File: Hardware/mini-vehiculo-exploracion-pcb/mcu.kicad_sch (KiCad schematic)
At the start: 20 parts, among them J3 UJ20-C-H-G-SMT-5-P16-TR

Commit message: update pcb4
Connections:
- net GND: now also J3.MP1, J3.MP2, J3.MP3, J3.MP4
- no-connect marks 10 -> 6
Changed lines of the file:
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@@
 	)
 	(junction
+		(at 69.85 110.49)
+		(diameter 0)
+		(color 0 0 0 0)
+	)
+	(junction
+		(at 69.85 113.03)
+		(diameter 0)
+		(color 0 0 0 0)
+	)
+	(junction
 		(at 77.47 33.02)
 		(diameter 0)
@@
 	)
 	(junction
+		(at 69.85 115.57)
+		(diameter 0)
+		(color 0 0 0 0)
+	)
+	(junction
 		(at 101.6 48.26)
 		(diameter 0)
@@
 	)
 	(no_connect
-		(at 67.31 110.49)
-	)
-	(no_connect
-		(at 67.31 115.57)
-	)
-	(no_connect
-		(at 67.31 113.03)
-	)
-	(no_connect
-		(at 67.31 107.95)
-	)
-	(no_connect
 		(at 71.12 55.88)
 	)
@@
 	(wire
 		(pts
+			(xy 69.85 110.49) (xy 69.85 113.03)
+		)
+		(stroke
+			(width 0)
+			(type default)
+		)
+	)
+	(wire
+		(pts
 			(xy 73.66 147.32) (xy 73.66 151.13)
 		)
@@
 	(wire
 		(pts
+			(xy 67.31 107.95) (xy 69.85 107.95)
+		)
+		(stroke
+			(width 0)
+			(type default)
+		)
+	)
+	(wire
+		(pts
 			(xy 67.31 102.87) (xy 71.12 102.87)
 		)
@@
 	(wire
 		(pts
+			(xy 69.85 107.95) (xy 69.85 110.49)
+		)
+		(stroke
+			(width 0)
+			(type default)
+		)
+	)
+	(wire
+		(pts
 			(xy 130.81 97.79) (xy 139.7 97.79)
 		)
@@
 	(wire
 		(pts
+			(xy 69.85 113.03) (xy 69.85 115.57)
+		)
+		(stroke
+			(width 0)
+			(type default)
+		)
+	)
+	(wire
+		(pts
 			(xy 101.6 62.23) (xy 104.14 62.23)
 		)
@@
 	(wire
 		(pts
+			(xy 69.85 115.57) (xy 69.85 118.11)
+		)
+		(stroke
+			(width 0)
+			(type default)
+		)
+	)
+	(wire
+		(pts
 			(xy 73.66 130.81) (xy 73.66 127)
 		)
@@
 	(wire
 		(pts
+			(xy 67.31 113.03) (xy 69.85 113.03)
+		)
+		(stroke
+			(width 0)
+			(type default)
+		)
+	)
+	(wire
+		(pts
 			(xy 137.16 118.11) (xy 137.16 120.65)
 		)
@@
 	(wire
 		(pts
+			(xy 67.31 110.49) (xy 69.85 110.49)
+		)
+		(stroke
+			(width 0)
+			(type default)
+		)
+	)
+	(wire
+		(pts
 			(xy 101.6 33.02) (xy 107.95 33.02)
 		)
@@
 	(wire
 		(pts
+			(xy 67.31 115.57) (xy 69.85 115.57)
+		)
+		(stroke
+			(width 0)
+			(type default)
+		)
+	)
+	(wire
+		(pts
 			(xy 77.47 113.03) (xy 85.09 113.03)
 		)
@@
 					(unit 1)
 				)
+			)
+		)
+	)
+	(symbol
+		(lib_id "power:GND")
+		(at 69.85 118.11 0)
+		(unit 1)
+		(exclude_from_sim no)
+		(in_bom yes)
+		(on_board yes)
+		(dnp no)
+		(fields_autoplaced yes)
+		(property "Reference" "#PWR013"
+			(at 69.85 124.46 0)
+			(effects
+				(font
+					(size 1.27 1.27)
+				)
+				(hide yes)
+			)
+		)
+		(property "Value" "GND"
+			(at 69.85 123.19 0)
+			(effects
+				(font
+					(size 1.27 1.27)
+				)
+			)
+		)
+		(property "Footprint" ""
+			(at 69.85 118.11 0)
+			(effects
+				(font
+					(size 1.27 1.27)
+				)
+				(hide yes)
+			)
+		)
+		(property "Datasheet" ""
+			(at 69.85 118.11 0)
+			(effects
+				(font
+					(size 1.27 1.27)
+				)
+				(hide yes)
+			)
+		)
+		(property "Description" "Power symbol creates a global label with name \"GND\" , ground"
+			(at 69.85 118.11 0)
+			(effects
+				(font
+					(size 1.27 1.27)
+				)
+				(hide yes)
+			)
+		)
+		(pin "1"
+		)
+		(instances
+			(project ""
+				(path "/3cb3b833-c38f-47b4-b7e9-f0e6337b7613/7b198334-65f4-4536-9697-14ad78bccec0"
+					(reference "#PWR013")
+					(unit 1)
+				)

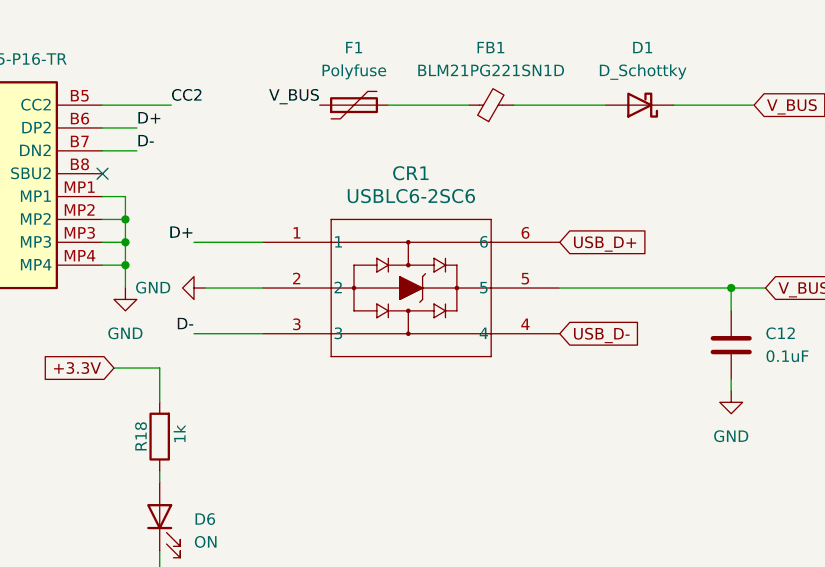
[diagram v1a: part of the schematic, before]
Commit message: Update USB layout and changed stackup
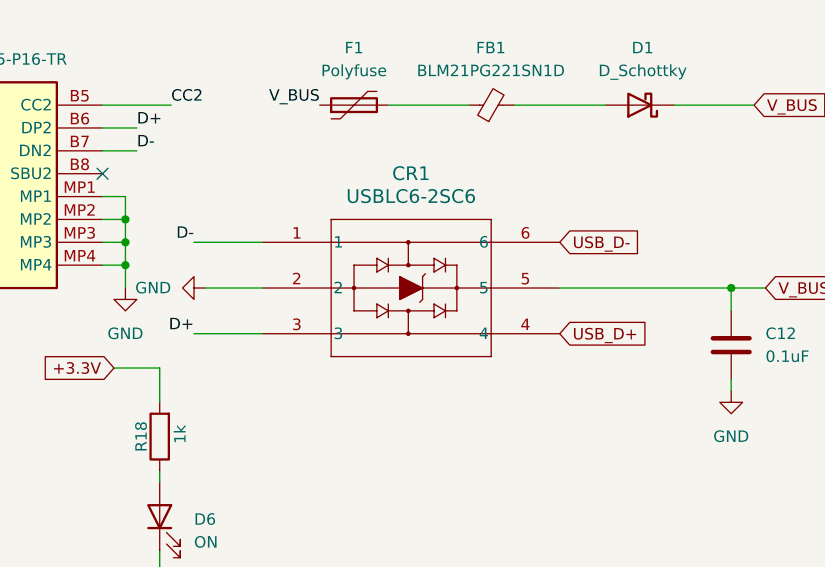
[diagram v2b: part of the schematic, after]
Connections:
- net D+: now also CR1.3; no longer CR1.1
- net D-: now also CR1.1; no longer CR1.3
- net USB_D+: now also CR1.4; no longer CR1.6
- net USB_D-: now also CR1.6; no longer CR1.4
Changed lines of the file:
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@@
 		)
 	)
-	(label "D-"
+	(label "D+"
 		(at 77.47 123.19 180)
 		(effects
@@
 		)
 	)
-	(label "D+"
+	(label "D-"
 		(at 77.47 113.03 180)
 		(effects
@@
 		)
 	)
+	(global_label "USB_D+"
+		(shape input)
+		(at 118.11 123.19 0)
+		(fields_autoplaced yes)
+		(effects
+			(font
+				(size 1.27 1.27)
+			)
+			(justify left)
+		)
+		(property "Intersheetrefs" "${INTERSHEET_REFS}"
+			(at 128.7152 123.19 0)
+			(effects
+				(font
+					(size 1.27 1.27)
+				)
+				(justify left)
+				(hide yes)
+			)
+		)
+	)
+	(global_label "ESP_IO0"
+		(shape input)
+		(at 195.58 53.34 0)
+		(fields_autoplaced yes)
+		(effects
+			(font
+				(size 1.27 1.27)
+			)
+			(justify left)
+		)
+		(property "Intersheetrefs" "${INTERSHEET_REFS}"
+			(at 206.3061 53.34 0)
+			(effects
+				(font
+					(size 1.27 1.27)
+				)
+				(justify left)
+				(hide yes)
+			)
+		)
+	)
+	(global_label "+3.3V"
+		(shape input)
+		(at 39.37 33.02 180)
+		(fields_autoplaced yes)
+		(effects
+			(font
+				(size 1.27 1.27)
+			)
+			(justify right)
+		)
+		(property "Intersheetrefs" "${INTERSHEET_REFS}"
+			(at 30.7 33.02 0)
+			(effects
+				(font
+					(size 1.27 1.27)
+				)
+				(justify right)
+				(hide yes)
+			)
+		)
+	)
+	(global_label "GND"
+		(shape input)
+		(at 25.4 113.03 180)
+		(fields_autoplaced yes)
+		(effects
+			(font
+				(size 1.27 1.27)
+			)
+			(justify right)
+		)
+		(property "Intersheetrefs" "${INTERSHEET_REFS}"
+			(at 18.5443 113.03 0)
+			(effects
+				(font
+					(size 1.27 1.27)
+				)
+				(justify right)
+				(hide yes)
+			)
+		)
+	)
+	(global_label "+3.3V"
+		(shape input)
+		(at 184.15 33.02 0)
+		(fields_autoplaced yes)
+		(effects
+			(font
+				(size 1.27 1.27)
+			)
+			(justify left)
+		)
+		(property "Intersheetrefs" "${INTERSHEET_REFS}"
+			(at 192.82 33.02 0)
+			(effects
+				(font
+					(size 1.27 1.27)
+				)
+				(justify left)
+				(hide yes)
+			)
+		)
+	)
 	(global_label "USB_D-"
 		(shape input)
-		(at 118.11 123.19 0)
-		(fields_autoplaced yes)
-		(effects
-			(font
-				(size 1.27 1.27)
-			)
-			(justify left)
-		)
-		(property "Intersheetrefs" "${INTERSHEET_REFS}"
-			(at 128.7152 123.19 0)
-			(effects
-				(font
-					(size 1.27 1.27)
-				)
-				(justify left)
-				(hide yes)
-			)
-		)
-	)
-	(global_label "ESP_IO0"
-		(shape input)
-		(at 195.58 53.34 0)
-		(fields_autoplaced yes)
-		(effects
-			(font
-				(size 1.27 1.27)
-			)
-			(justify left)
-		)
-		(property "Intersheetrefs" "${INTERSHEET_REFS}"
-			(at 206.3061 53.34 0)
-			(effects
-				(font
-					(size 1.27 1.27)
-				)
-				(justify left)
-				(hide yes)
-			)
-		)
-	)
-	(global_label "+3.3V"
-		(shape input)
-		(at 39.37 33.02 180)
-		(fields_autoplaced yes)
-		(effects
-			(font
-				(size 1.27 1.27)
-			)
-			(justify right)
-		)
-		(property "Intersheetrefs" "${INTERSHEET_REFS}"
-			(at 30.7 33.02 0)
-			(effects
-				(font
-					(size 1.27 1.27)
-				)
-				(justify right)
-				(hide yes)
-			)
-		)
-	)
-	(global_label "GND"
-		(shape input)
-		(at 25.4 113.03 180)
-		(fields_autoplaced yes)
-		(effects
-			(font
-				(size 1.27 1.27)
-			)
-			(justify right)
-		)
-		(property "Intersheetrefs" "${INTERSHEET_REFS}"
-			(at 18.5443 113.03 0)
-			(effects
-				(font
-					(size 1.27 1.27)
-				)
-				(justify right)
-				(hide yes)
-			)
-		)
-	)
-	(global_label "+3.3V"
-		(shape input)
-		(at 184.15 33.02 0)
-		(fields_autoplaced yes)
-		(effects
-			(font
-				(size 1.27 1.27)
-			)
-			(justify left)
-		)
-		(property "Intersheetrefs" "${INTERSHEET_REFS}"
-			(at 192.82 33.02 0)
-			(effects
-				(font
-					(size 1.27 1.27)
-				)
-				(justify left)
-				(hide yes)
-			)
-		)
-	)
-	(global_label "USB_D+"
-		(shape input)
 		(at 118.11 113.03 0)
